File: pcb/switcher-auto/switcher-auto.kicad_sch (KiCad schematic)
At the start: 36 parts, among them J0 MD-90SM, J5 Conn_02x22_Top_Bottom, SW1 SW_Push, SW2 SW_Push, U1 CD74HC4067SM96, U11 THS7374, U2 CD74HC4067SM96, U3 CD74HC4067SM96, U4 CD74HC4067SM96, U5 CD74HC4067SM96, U6 CD74HC4067SM96, U7 CD74HC4067SM96

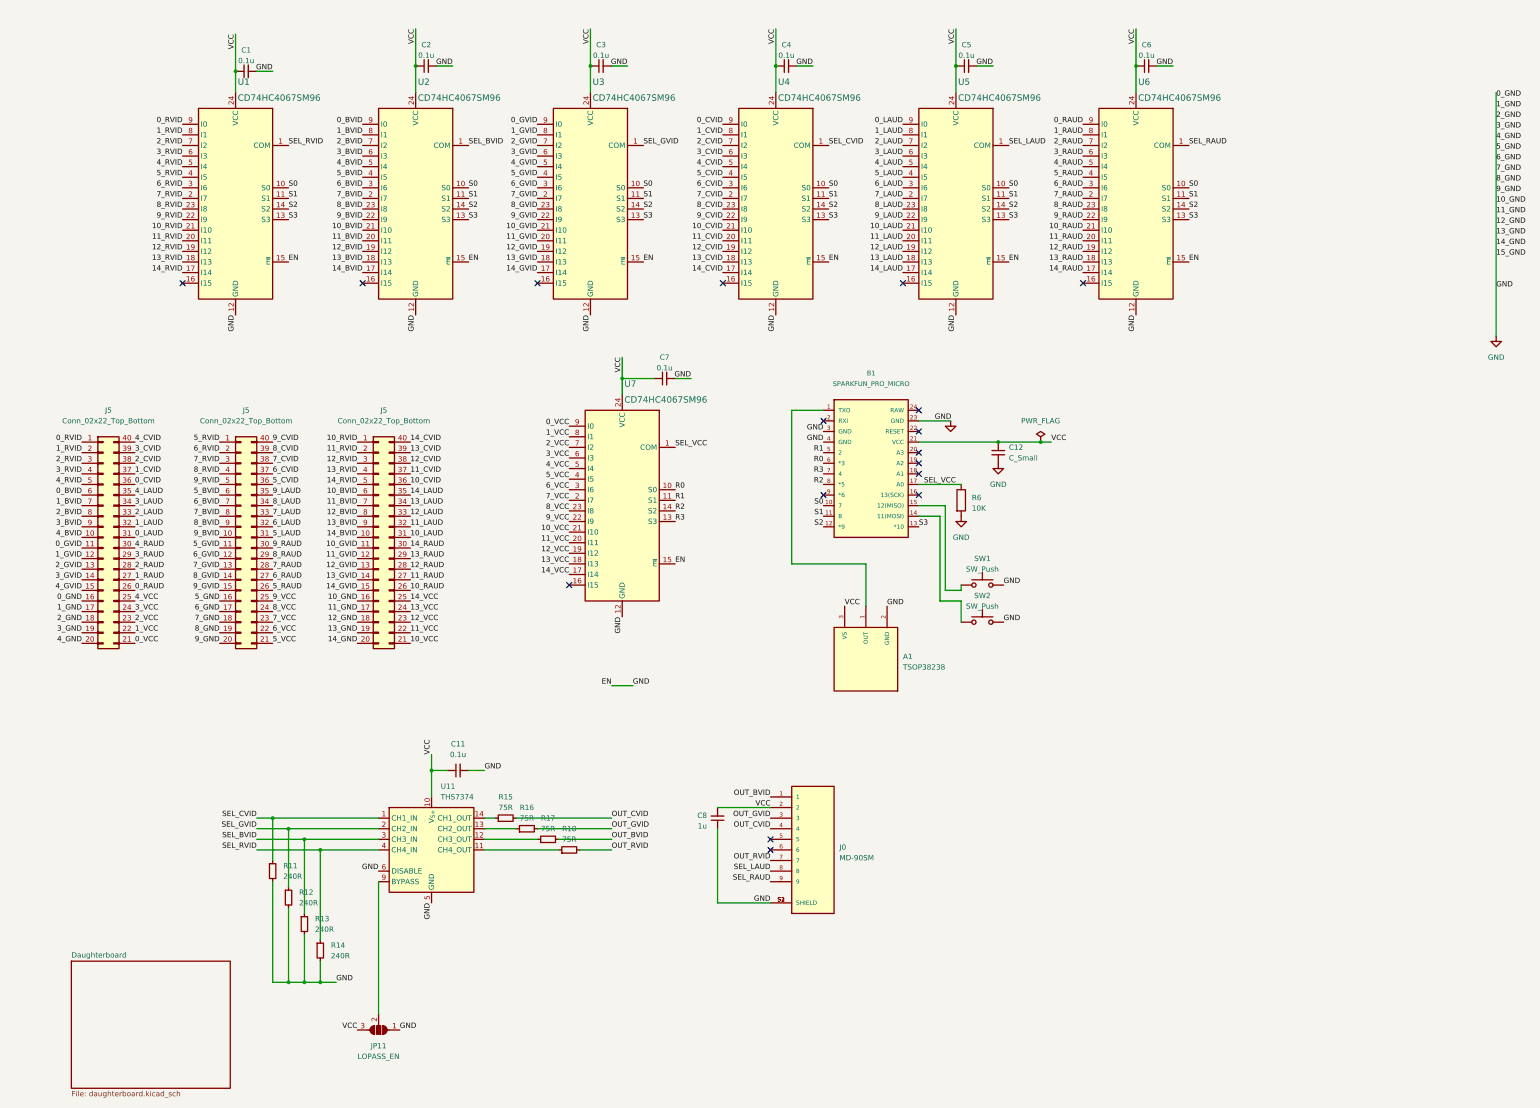
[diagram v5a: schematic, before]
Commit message: WIP dual supply audio switching
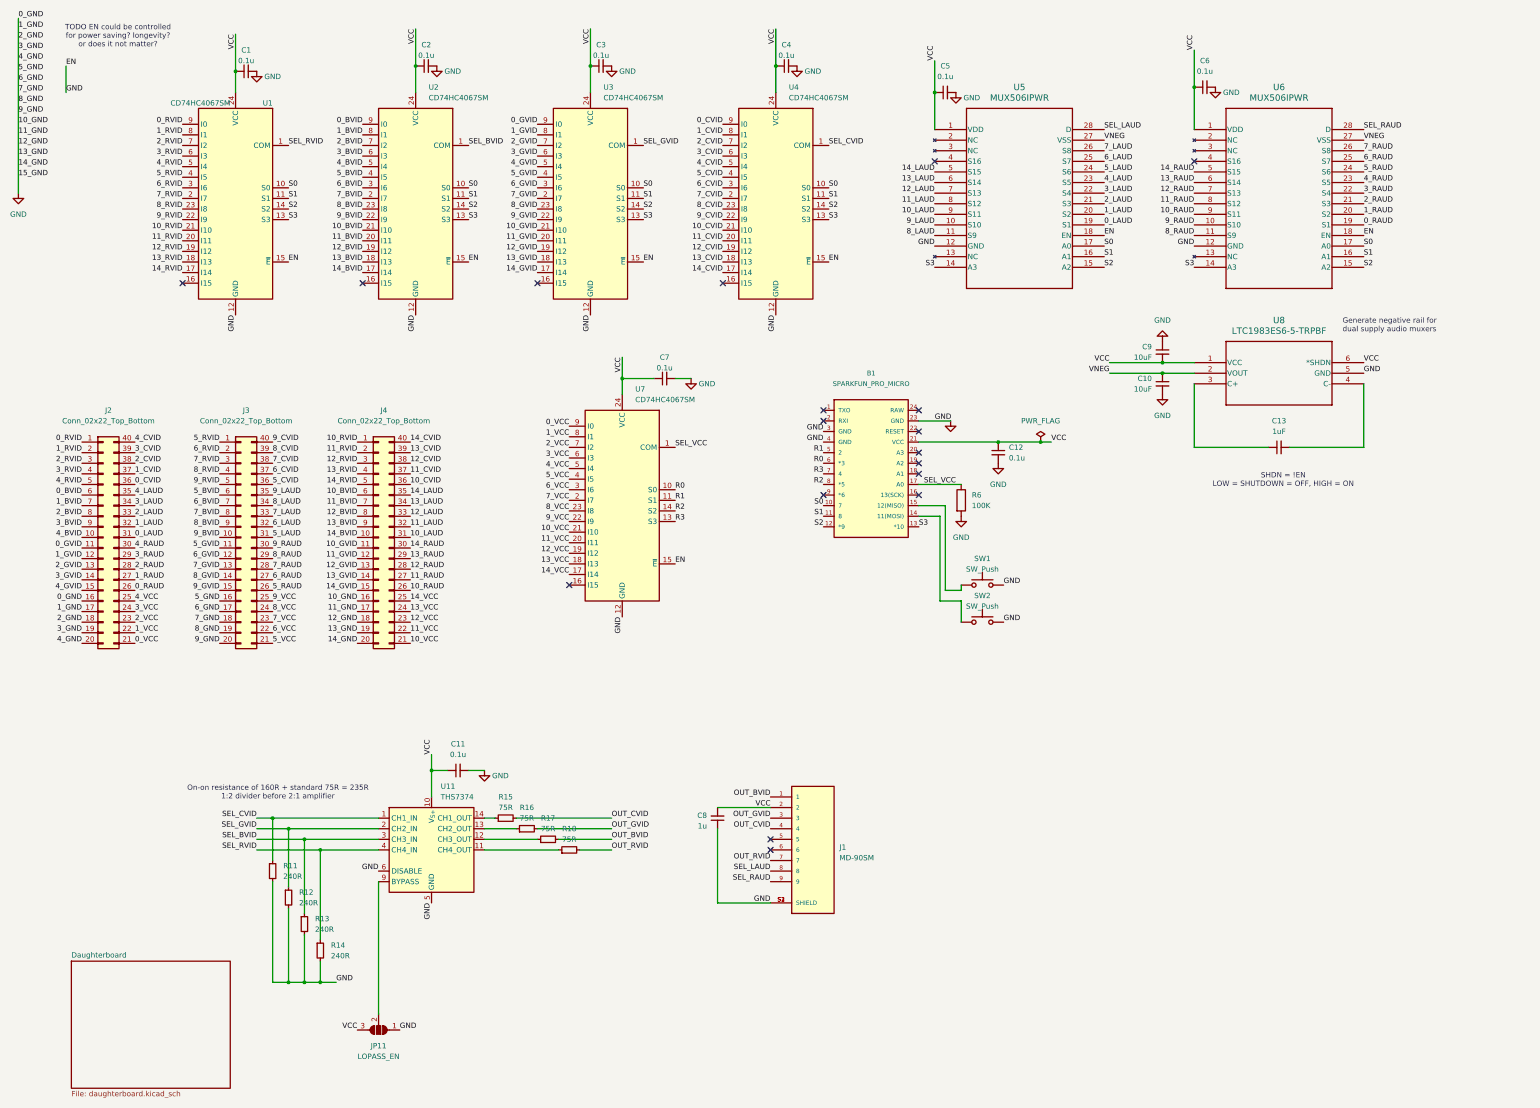
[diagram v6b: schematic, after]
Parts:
- removed A1: TSOP38238, REB-IR:XDCR_TSOP38238, symbol REB-IR:TSOP38238
- removed U5, U6: CD74HC4067SM96, Package_SO:SOIC-24W_7.5x15.4mm_P1.27mm, symbol REB-DIN:CD4067BM96
- added C10, C9: 10uF, Capacitor_SMD:C_0805_2012Metric_Pad1.18x1.45mm_HandSolder, symbol Device:C_Small
- added C13: 1uF, Capacitor_SMD:C_0805_2012Metric_Pad1.18x1.45mm_HandSolder, symbol Device:C_Small
- added U5, U6: MUX506IPWR, REB-MUX:PW28_TEX, symbol REB-MUX:MUX506IPWR
- added U8: LTC1983ES6-5-TRPBF, REB-LTC:LTC1983ES6-5-TRPBF_ADI, symbol REB-LTC:LTC1983ES6-5-TRPBF
- C12: value C_Small -> 0.1u
- R6: value 10K -> 100K
- U1, U2, U3, U4, U7: value CD74HC4067SM96 -> CD74HC4067SM; footprint Package_SO:SOIC-24W_7.5x15.4mm_P1.27mm -> Package_SO:SSOP-24_5.3x8.2mm_P0.65mm; symbol REB-DIN:CD4067BM96 -> 74xx:CD74HC4067SM
- renumbered J0 to J1, J5 to J2, J5 to J3, J5 to J4
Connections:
- net 0_LAUD: now also U5.19 (S1)
- net 0_RAUD: now also U6.19 (S1)
- net 10_LAUD: now also U5.9 (S11)
- net 10_RAUD: now also U6.9 (S11)
- net 11_LAUD: now also U5.8 (S12)
- net 11_RAUD: now also U6.8 (S12)
- net 12_LAUD: now also U5.7 (S13)
- net 12_RAUD: now also U6.7 (S13)
- net 13_LAUD: now also U5.6 (S14)
- net 13_RAUD: now also U6.6 (S14)
- net 14_LAUD: now also U5.5 (S15)
- net 14_RAUD: now also U6.5 (S15)
- net 1_LAUD: now also U5.20 (S2)
- net 1_RAUD: now also U6.20 (S2)
- net 2_LAUD: now also U5.21 (S3)
- net 2_RAUD: now also U6.21 (S3)
- net 3_LAUD: now also U5.22 (S4)
- net 3_RAUD: now also U6.22 (S4)
- net 4_LAUD: now also U5.23 (S5)
- net 4_RAUD: now also U6.23 (S5)
- net 5_LAUD: now also U5.24 (S6)
- net 5_RAUD: now also U6.24 (S6)
- net 6_LAUD: now also U5.25 (S7)
- net 6_RAUD: now also U6.25 (S7)
- net 7_LAUD: now also U5.26 (S8)
- net 7_RAUD: now also U6.26 (S8)
- net 8_LAUD: now also U5.11 (S9)
- net 8_RAUD: now also U6.11 (S9)
- net 9_LAUD: now also U5.10 (S10)
- net 9_RAUD: now also U6.10 (S10)
- net GND: now also C10.2, C9.1, U5.12 (GND), U5.18 (EN), U6.12 (GND), U6.18 (EN), U8.5 (GND)
- net S0: now also U5.17 (A0), U6.17 (A0)
- net S1: now also U5.16 (A1), U6.16 (A1)
- net S2: now also U5.15 (A2), U6.15 (A2)
- net S3: now also U5.14 (A3), U6.14 (A3)
- net SEL_LAUD: now also U5.28 (D)
- net SEL_RAUD: now also U6.28 (D)
- net VCC: now also C9.2, U5.1 (VDD), U6.1 (VDD), U8.1 (VCC), U8.6 (*SHDN)
- new net: C13.1, U8.3 (C+)
- new net: C13.2, U8.4 (C-)
- new net VNEG: C10.1, U5.27 (VSS), U6.27 (VSS), U8.2 (VOUT)
- no-connect marks 17 -> 18
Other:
- note added: "Generate negative rail for dual supply audio muxers"
- note added: "On-on resistance of 160R + standard 75R = 235R 1:2 divider before 2:1 amplifier"
- note added: "SHDN = !EN LOW = SHUTDOWN = OFF, HIGH = ON"
- note added: "TODO EN could be controlled for power saving? longevity? or does it not matter?"

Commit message: Routing checkpoint
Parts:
- removed U8: LTC1983ES6-5-TRPBF, REB-LTC:LTC1983ES6-5-TRPBF_ADI, symbol REB-LTC:LTC1983ES6-5-TRPBF
- added C14: 1uF, Capacitor_SMD:C_0805_2012Metric_Pad1.18x1.45mm_HandSolder, symbol Device:C_Polarized_Small
- added C15: 0.1u, Capacitor_SMD:C_0805_2012Metric_Pad1.18x1.45mm_HandSolder, symbol Device:C_Small
- added U8: LM2776, Package_TO_SOT_SMD:SOT-23-6, symbol Regulator_SwitchedCapacitor:LM2776
- C10, C9: value 10uF -> 2.2uF
- C13: value 1uF -> 0.1u
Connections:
- net VNEG is gone; now on net -5V: C10.1, U5.27 (VSS), U6.27 (VSS)
- net 0_LAUD: now also U5.11 (S9); no longer U5.19 (S1)
- net 0_RAUD: now also U6.11 (S9); no longer U6.19 (S1)
- net 10_LAUD: now also U5.24 (S6); no longer U5.9 (S11)
- net 10_RAUD: now also U6.24 (S6); no longer U6.9 (S11)
- net 11_LAUD: now also U5.23 (S5); no longer U5.8 (S12)
- net 11_RAUD: now also U6.23 (S5); no longer U6.8 (S12)
- net 12_LAUD: now also U5.22 (S4); no longer U5.7 (S13)
- net 12_RAUD: now also U6.22 (S4); no longer U6.7 (S13)
- net 13_LAUD: now also U5.21 (S3); no longer U5.6 (S14)
- net 13_RAUD: now also U6.21 (S3); no longer U6.6 (S14)
- net 14_LAUD: now also U5.20 (S2); no longer U5.5 (S15)
- net 14_RAUD: now also U6.20 (S2); no longer U6.5 (S15)
- net 1_LAUD: now also U5.10 (S10); no longer U5.20 (S2)
- net 1_RAUD: now also U6.10 (S10); no longer U6.20 (S2)
- net 2_LAUD: now also U5.9 (S11); no longer U5.21 (S3)
- net 2_RAUD: now also U6.9 (S11); no longer U6.21 (S3)
- net 3_LAUD: now also U5.8 (S12); no longer U5.22 (S4)
- net 3_RAUD: now also U6.8 (S12); no longer U6.22 (S4)
- net 4_LAUD: now also U5.7 (S13); no longer U5.23 (S5)
- net 4_RAUD: now also U6.7 (S13); no longer U6.23 (S5)
- net 5_LAUD: now also U5.6 (S14); no longer U5.24 (S6)
- net 5_RAUD: now also U6.6 (S14); no longer U6.24 (S6)
- net 6_LAUD: now also U5.5 (S15); no longer U5.25 (S7)
- net 6_RAUD: now also U6.5 (S15); no longer U6.25 (S7)
- net 7_LAUD: now also U5.4 (S16); no longer U5.26 (S8)
- net 7_RAUD: now also U6.4 (S16); no longer U6.26 (S8)
- net 8_LAUD: now also U5.26 (S8); no longer U5.11 (S9)
- net 8_RAUD: now also U6.26 (S8); no longer U6.11 (S9)
- net 9_LAUD: now also U5.25 (S7); no longer U5.10 (S10)
- net 9_RAUD: now also U6.25 (S7); no longer U6.10 (S10)
- net GND: now also C13.2, C15.2, U8.2 (GND)
- net R0: no longer B1.6 (*3)
- net R1: no longer B1.5 (2)
- net R2: no longer B1.8 (*5)
- net R3: no longer B1.7 (4)
- net S0: no longer U5.17 (A0), U6.17 (A0)
- net S1: no longer U5.16 (A1), U6.16 (A1)
- net S2: no longer U5.15 (A2), U6.15 (A2)
- net S3: no longer U5.14 (A3), U6.14 (A3)
- net VCC: now also U8.3 (VIN), U8.4 (EN)
- net -5V: now reaches C13.1
- net -5V: now also C15.1, U8.1 (VOUT)
- new net: C14.1, U8.5 (C1+)
- new net: C14.2, U8.6 (C1-)
- new net AUDSEL0: B1.5 (2), U5.17 (A0), U6.17 (A0)
- new net AUDSEL1: B1.6 (*3), U5.16 (A1), U6.16 (A1)
- new net AUDSEL2: B1.7 (4), U5.15 (A2), U6.15 (A2)
- new net AUDSEL3: U5.14 (A3), U6.14 (A3)
- no-connect marks 18 -> 19
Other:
- note added: "NOTE! Using a different mapping to avoid rerouting"
- note removed: "SHDN = !EN LOW = SHUTDOWN = OFF, HIGH = ON"
- moved on the sheet: B1, C10, C12, C9, R6, SW1, SW2

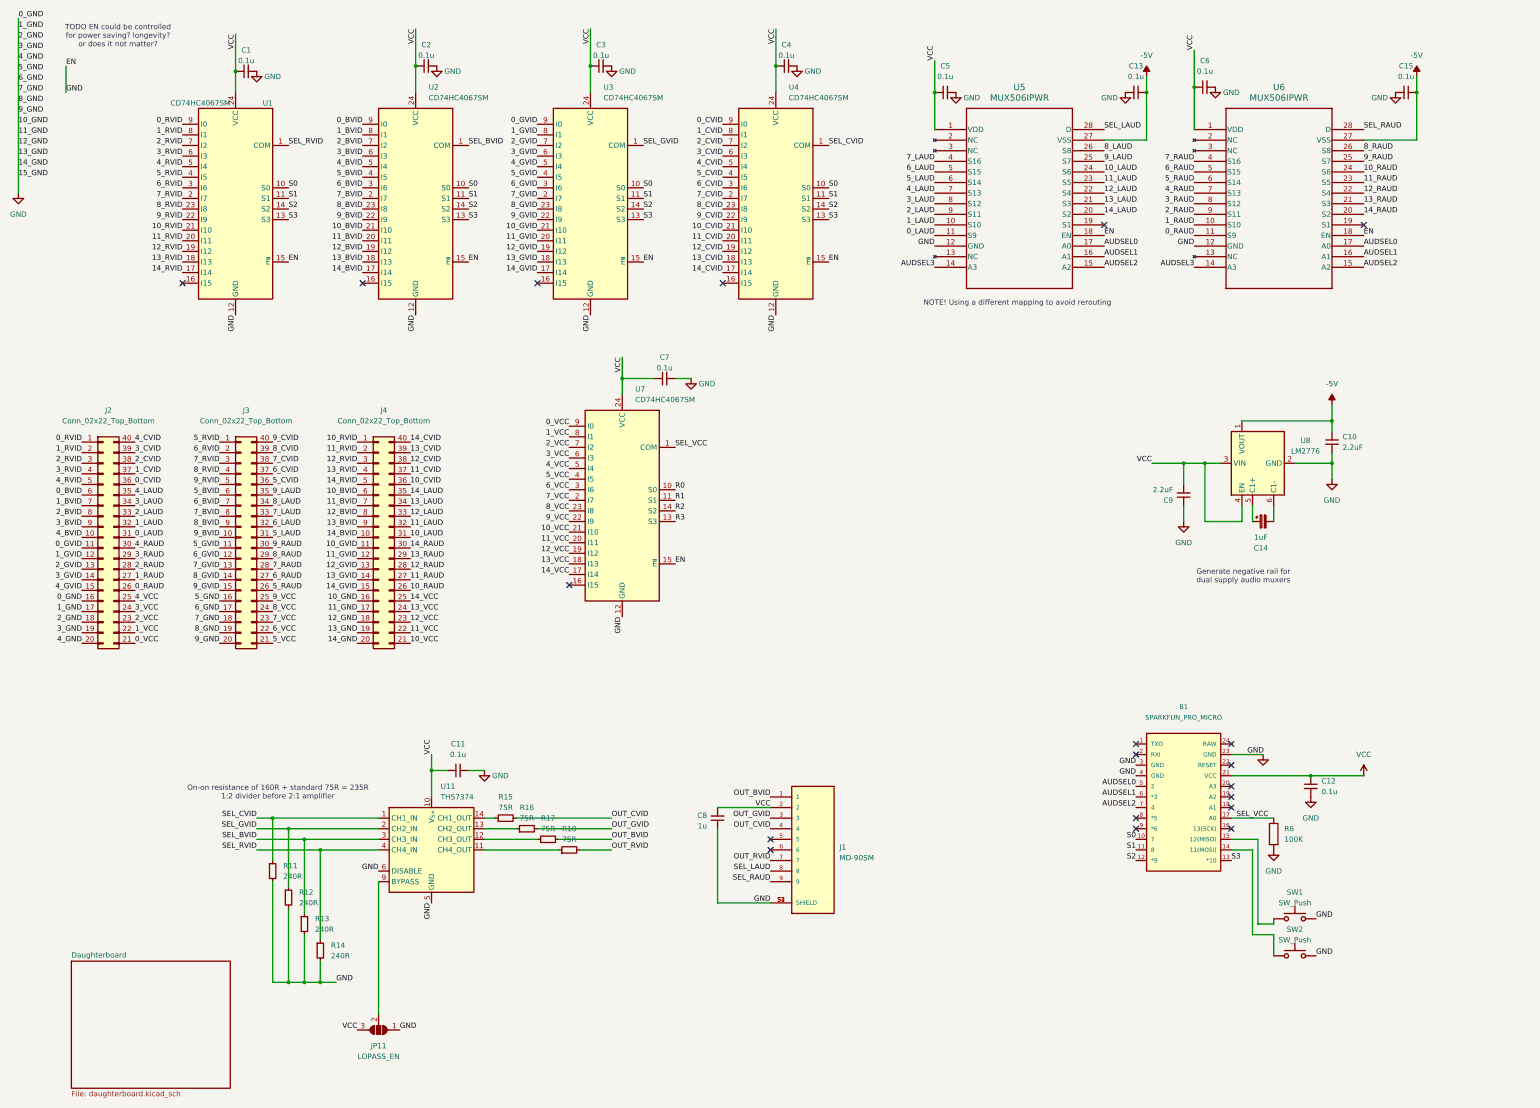
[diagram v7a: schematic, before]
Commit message: Cleared up one layer for solid ground plane
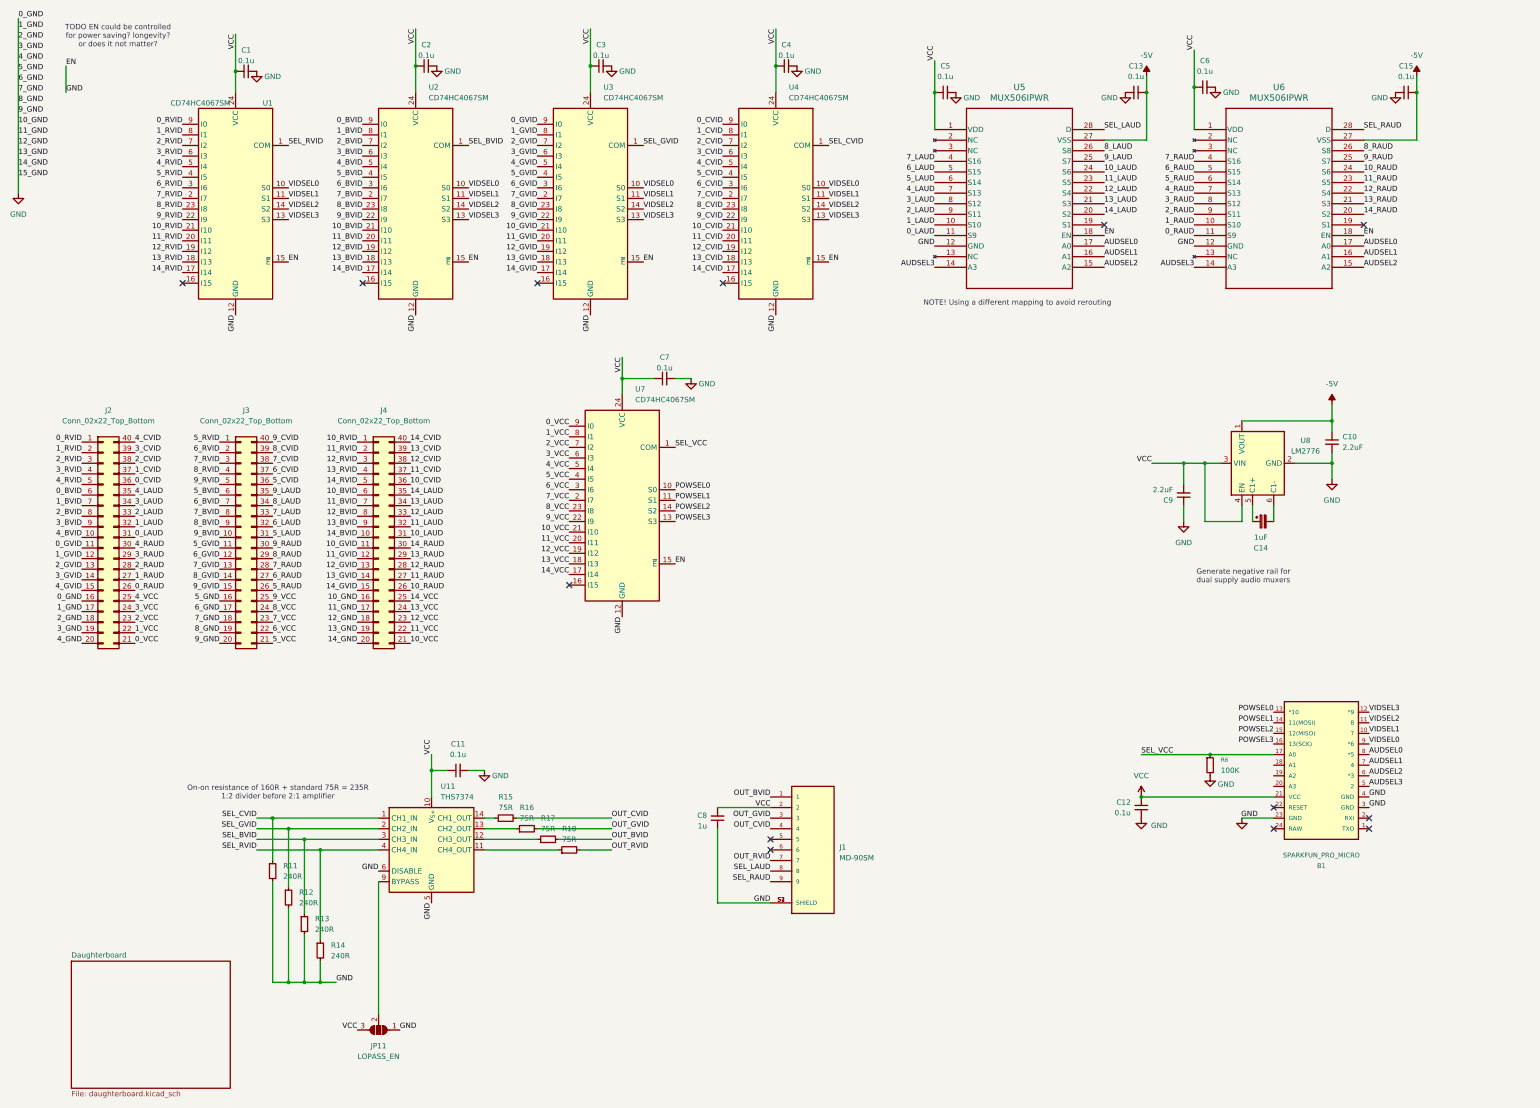
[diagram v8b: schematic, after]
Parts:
- removed R6: 100K, Resistor_SMD:R_0805_2012Metric_Pad1.20x1.40mm_HandSolder, symbol Device:R
- removed SW1, SW2: SW_Push, Button_Switch_THT:SW_PUSH_6mm, symbol Switch:SW_Push
- added R6: 100K, symbol Device:R_Small
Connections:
- net R1 is gone; now on net POWSEL1: U7.11 (S1)
- net R2 is gone; now on net POWSEL2: U7.14 (S2)
- net R3 is gone; now on net POWSEL3: U7.13 (S3)
- net AUDSEL0: now also B1.8 (*5); no longer B1.5 (2)
- net AUDSEL1: now also B1.7 (4); no longer B1.6 (*3)
- net AUDSEL2: now also B1.6 (*3); no longer B1.7 (4)
- net AUDSEL3: now also B1.5 (2)
- net GND: now also R6.2
- net SEL_VCC: now also R6.1
- net POWSEL1: now reaches B1.14 (11(MOSI))
- net POWSEL2: now reaches B1.15 (12(MISO))
- net POWSEL3: now reaches B1.16 (13(SCK))
- net VIDSEL0: now reaches B1.9 (*6)
- net VIDSEL0: now also U1.10 (S0), U2.10 (S0), U3.10 (S0), U4.10 (S0)
- net R0 renamed POWSEL0
- net POWSEL0: now also B1.13 (*10)
- removed net S0: B1.10 (7), U1.10 (S0), U2.10 (S0), U3.10 (S0), U4.10 (S0)
- net S1 renamed VIDSEL1
- net VIDSEL1: now also B1.10 (7); no longer B1.11 (8)
- net S2 renamed VIDSEL2
- net VIDSEL2: now also B1.11 (8); no longer B1.12 (*9)
- net S3 renamed VIDSEL3
- net VIDSEL3: now also B1.12 (*9); no longer B1.13 (*10)
- no-connect marks 19 -> 13
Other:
- moved on the sheet: B1, C12
